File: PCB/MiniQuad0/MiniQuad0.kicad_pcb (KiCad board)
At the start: 2 copper layers, 36 x 50 mm, 30 parts, among them J1 R8EF_Radio, J10 BMP280_breakout, J11 HMC5883L_breakout, J12 MAG_drdy, J13 BAR_CSB, J14 BAR_SD0, J15 MCU_BOOT, J16 MCU_RST, J17 MCU_SWDIO, J2 POWER, J3 ESC_A, J4 ESC_B, J5 ESC_C, J6 ESC_D, J7 POWER, J8 VBAT, J9 RADIO_SIG, Q1 2N2222, U1 LSM6DSOTR, U2 XIAO-RP2350-SMD

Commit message: changed pin defs, finished PCB
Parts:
- moved J9 26.9 mm to (159.0, 127.1)
- moved R3 1.25 mm to (162.8, 124.7)
- moved R4 1.25 mm to (162.8, 127.1)
- moved R1 1.05 mm to (152.5, 101.9)
- moved J3 0.50 mm to (143.8, 89.2)
- moved J4 0.50 mm to (152.2, 89.2)
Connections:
- U2 pad 1: /BAT_SENSE -> /MOTOR_C
- U2 pad 10: /IMU_SD0 -> unconnected-(U2-GPIO4/D9/SPI0_MISO-Pad10)
- U2 pad 11: /IMU_SDA -> /MOTOR_D
- U2 pad 15: unconnected-(U2-GPIO21/D11/RX1-Pad15) -> /IMU_INT2
- U2 pad 16: unconnected-(U2-GPIO20/D12/TX1-Pad16) -> /IMU_INT1
- U2 pad 17: /IMU_I2C_SCL -> unconnected-(U2-GPIO17/D13/SCL0-Pad17)
- U2 pad 18: /IMU_I2C_SDA -> unconnected-(U2-GPIO16/D14/SDA0-Pad18)
- U2 pad 19: unconnected-(U2-GPIO11/D15/SPI1_MOSI-Pad19) -> /IMU_SDA
- U2 pad 2: /MOTOR_A -> /BAT_SENSE
- U2 pad 20: /IMU_INT1 -> /IMU_SD0
- U2 pad 21: /IMU_INT2 -> /IMU_SCL
- U2 pad 22: /RADIO_SIG -> /IMU_CS
- U2 pad 3: /MOTOR_B -> /RADIO_SIG
- U2 pad 4: /MOTOR_C -> /MOTOR_B
- U2 pad 5: /MOTOR_D -> /IMU_I2C_SDA
- U2 pad 6: /IMU_SD0 -> /IMU_I2C_SCL
- U2 pad 9: /IMU_SCL -> /MOTOR_A
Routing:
- net +5V: track 0.00 -> 59.9 mm, vias 0 -> 1
- net /IMU_I2C_SDA: track 0.00 -> 55.4 mm
- net /IMU_I2C_SCL: track 0.00 -> 51.6 mm, vias 0 -> 1
- net /MOTOR_B: track 0.00 -> 42.0 mm, vias 0 -> 3
- net /RADIO_SIG: track 0.00 -> 38.6 mm, vias 0 -> 2
- net /MOTOR_A: track 0.00 -> 34.7 mm, vias 0 -> 1
- net /IMU_CS: track 0.00 -> 30.9 mm, vias 0 -> 2
- net /IMU_INT2: track 0.00 -> 30.4 mm
- net /IMU_SD0: track 0.00 -> 27.3 mm, vias 0 -> 2
- net /IMU_SCL: track 0.00 -> 26.7 mm, vias 0 -> 2
- net /IMU_INT1: track 0.00 -> 23.6 mm
- net /IMU_SDA: track 0.00 -> 21.1 mm, vias 0 -> 2
- net +3.3V: track 0.00 -> 16.7 mm, vias 0 -> 4
- net Net-(Q1-B): track 0.00 -> 10.4 mm
- net GND: track 0.00 -> 9.97 mm, vias 0 -> 46
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- added copper zone on In2.Cu, net +3.3V
- added copper zone on B.Cu, net GND
- added copper zone on F.Cu, net GND
- added copper zone on In1.Cu, net GND
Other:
- board size 36 x 50 mm -> 38.5 x 51.2 mm
- copper layers 2 -> 4
- board text added: "+5V"
- board text added: "3V3"
- board text added: "5V"
- board text added: "GND"
- board text added: "M_A"
- board text added: "M_B"
- board text added: "M_C"
- board text added: "M_D"
- board text added: "PWR"
- board text added: "PWR-IN"
- board text added: "RADIO"
- board text added: "VCC"

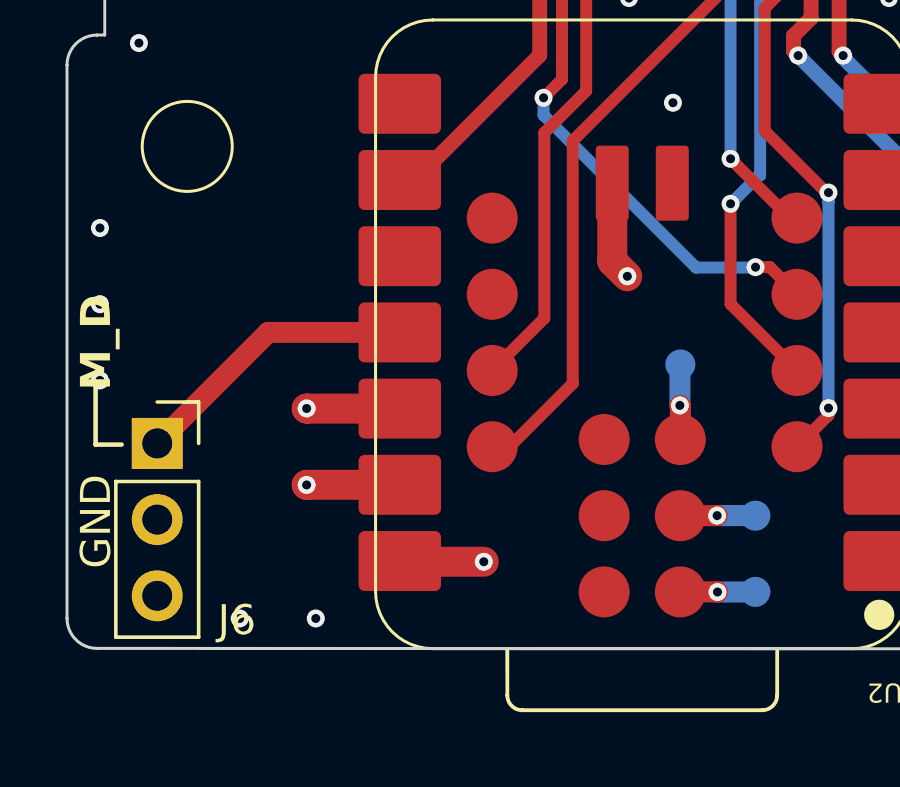
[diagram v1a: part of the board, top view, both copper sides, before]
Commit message: added test pads for unused pins under the mcu which were inaccessible otherwise
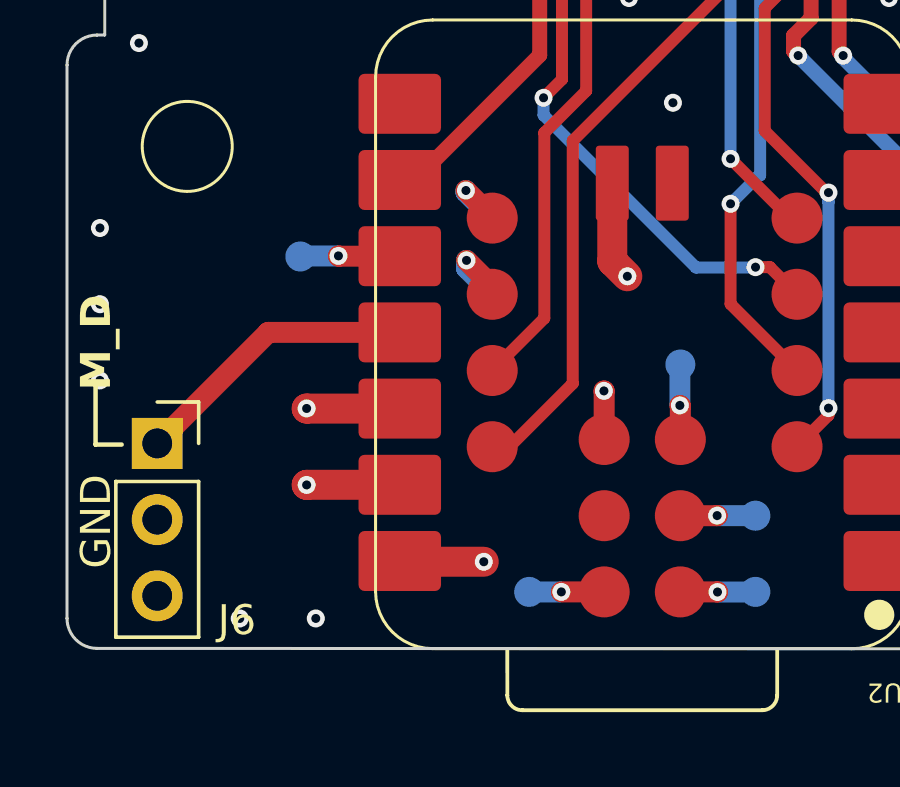
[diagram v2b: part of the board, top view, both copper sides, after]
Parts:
- added J18: MCU_SWDCLK, TestPoint:TestPoint_Pad_D1.0mm, B.Cu at (144.1, 135.1)
- added J19: MCU_GP17, TestPoint:TestPoint_Pad_D1.0mm, B.Cu at (142.9, 125.2)
- added J20: MCU_GP16, TestPoint:TestPoint_Pad_D1.0mm, B.Cu at (142.9, 122.6)
- added J21: MCU_GP04, TestPoint:TestPoint_Pad_D1.0mm, B.Cu at (136.5, 123.9)
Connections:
- U2 pad 10: unconnected-(U2-GPIO4/D9/SPI0_MISO-Pad10) -> Net-(J21-Pin_1)
- U2 pad 17: unconnected-(U2-GPIO17/D13/SCL0-Pad17) -> Net-(J19-Pin_1)
- U2 pad 18: unconnected-(U2-GPIO16/D14/SDA0-Pad18) -> Net-(J20-Pin_1)
- U2 pad 26: unconnected-(U2-3V3_1-Pad26) -> +3.3V
- U2 pad 28: unconnected-(U2-SWDCLK-Pad28) -> Net-(J18-Pin_1)
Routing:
- net Net-(J21-Pin_1): track 0.00 -> 3.33 mm, vias 0 -> 1
- net Net-(J19-Pin_1): track 0.00 -> 2.95 mm, vias 0 -> 1
- net Net-(J20-Pin_1): track 0.00 -> 2.56 mm, vias 0 -> 1
- net Net-(J18-Pin_1): track 0.00 -> 2.50 mm, vias 0 -> 1
- net +3.3V: track 16.7 -> 18.4 mm, vias 4 -> 5
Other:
- board text added: "GP04"
- board text added: "GP16"
- board text added: "GP17"
- board text added: "SWDCLK"
- board text added: "SWDIO"
- board text removed: "MCU_SWDIO"
